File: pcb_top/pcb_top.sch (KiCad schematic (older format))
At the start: 37 parts, among them J1 Screw_Terminal_1x02, J10 Screw_Terminal_1x03, J2 Screw_Terminal_1x02, J3 Screw_Terminal_1x02, J4 Screw_Terminal_1x02, J5 Screw_Terminal_1x03, J6 Screw_Terminal_1x03, J7 Screw_Terminal_1x03, J8 Screw_Terminal_1x03, J9 CONN_02X04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

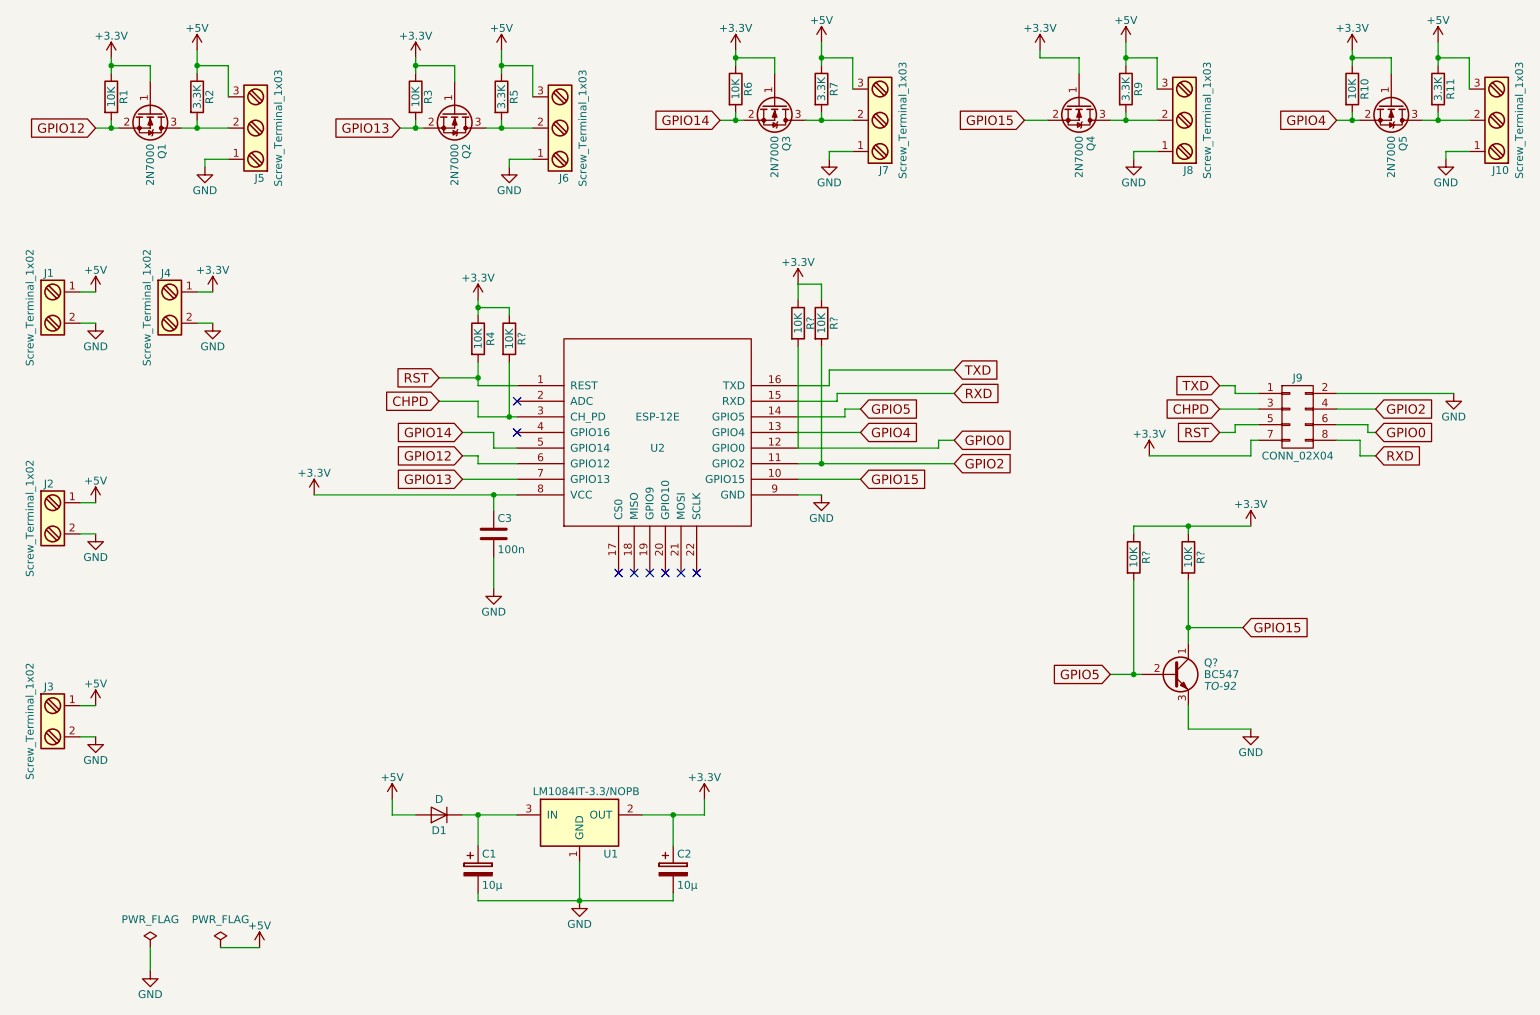
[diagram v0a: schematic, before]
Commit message: Update top-pcb schematic
Signed-off-by: Jan Losinski <losinski@wh2.tu-dresden.de>
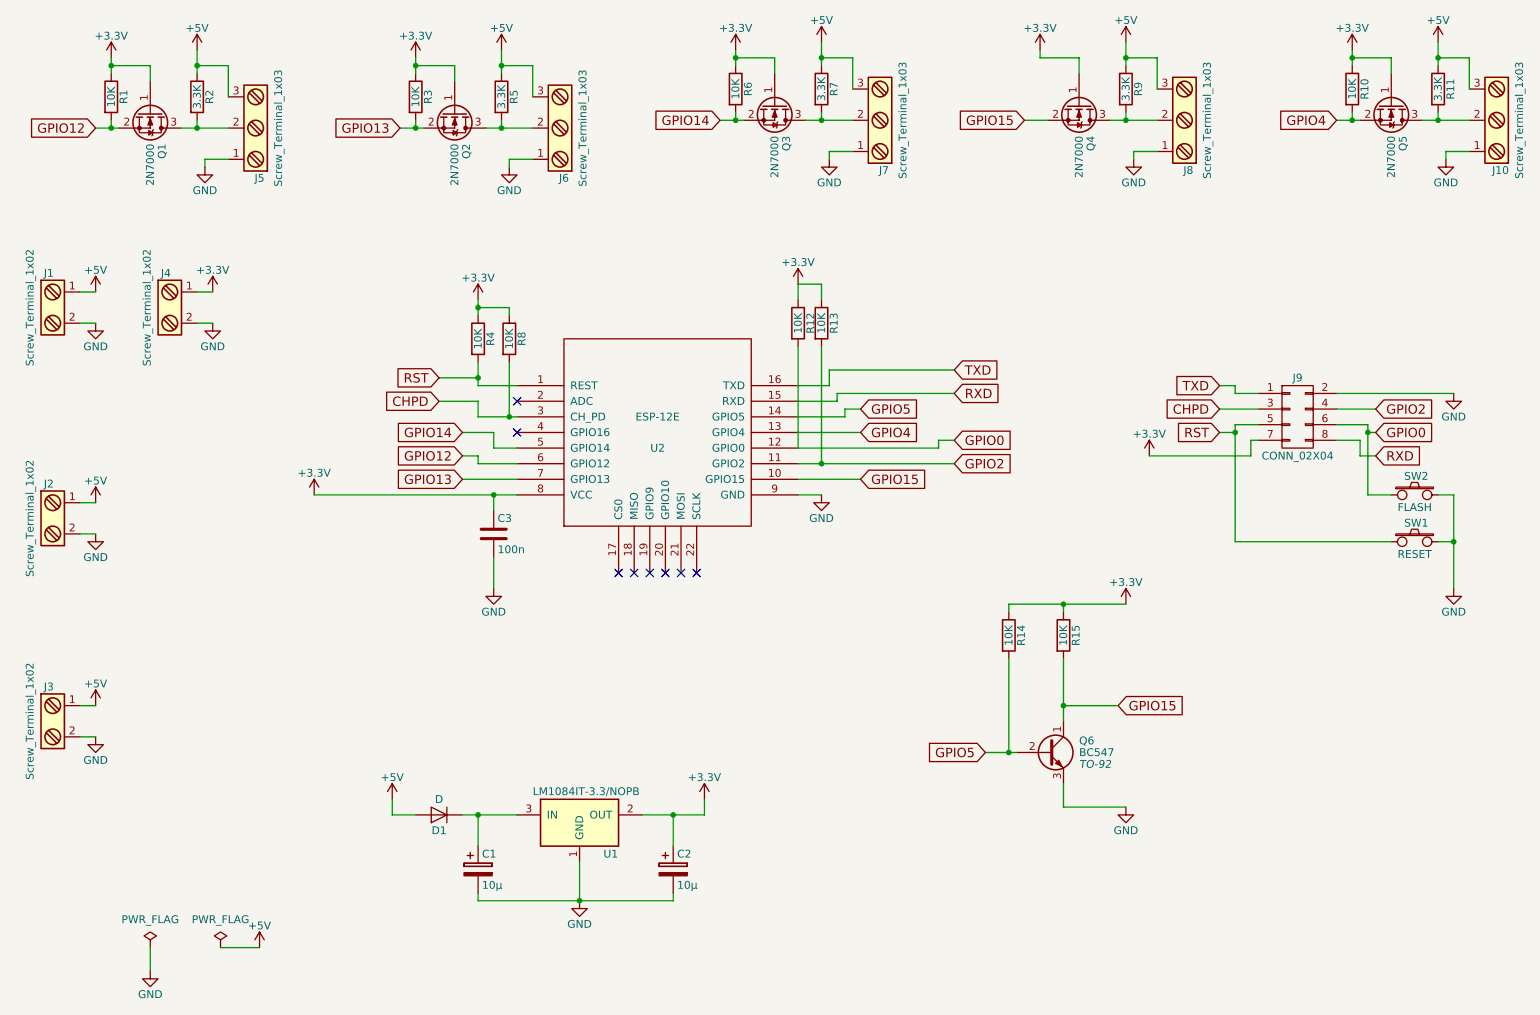
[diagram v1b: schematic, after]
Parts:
- added SW1: RESET, symbol SW_PUSH
- added SW2: FLASH, symbol SW_PUSH
- gave numbers to parts that had none: 6
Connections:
- net GND: now also SW1.2, SW2.2
- net GPIO0: now also SW2.1
- net RST: now also SW1.1
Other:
- moved on the sheet: Q6, R14, R15
